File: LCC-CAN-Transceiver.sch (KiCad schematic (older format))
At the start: 19 parts

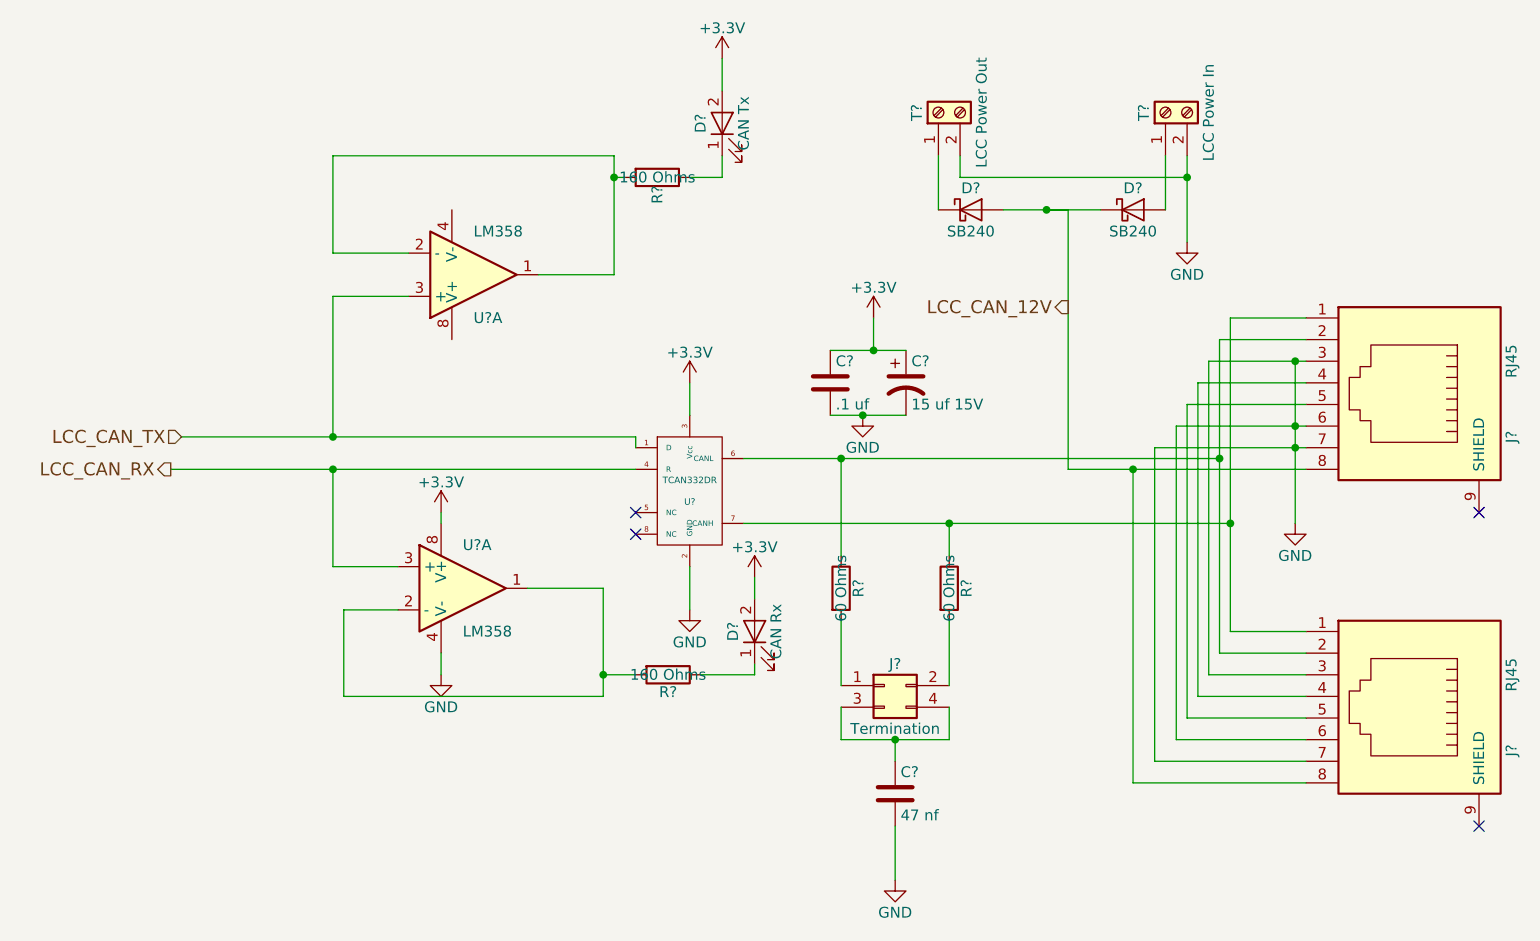
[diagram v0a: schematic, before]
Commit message: Start on LCC <=> PNET router.
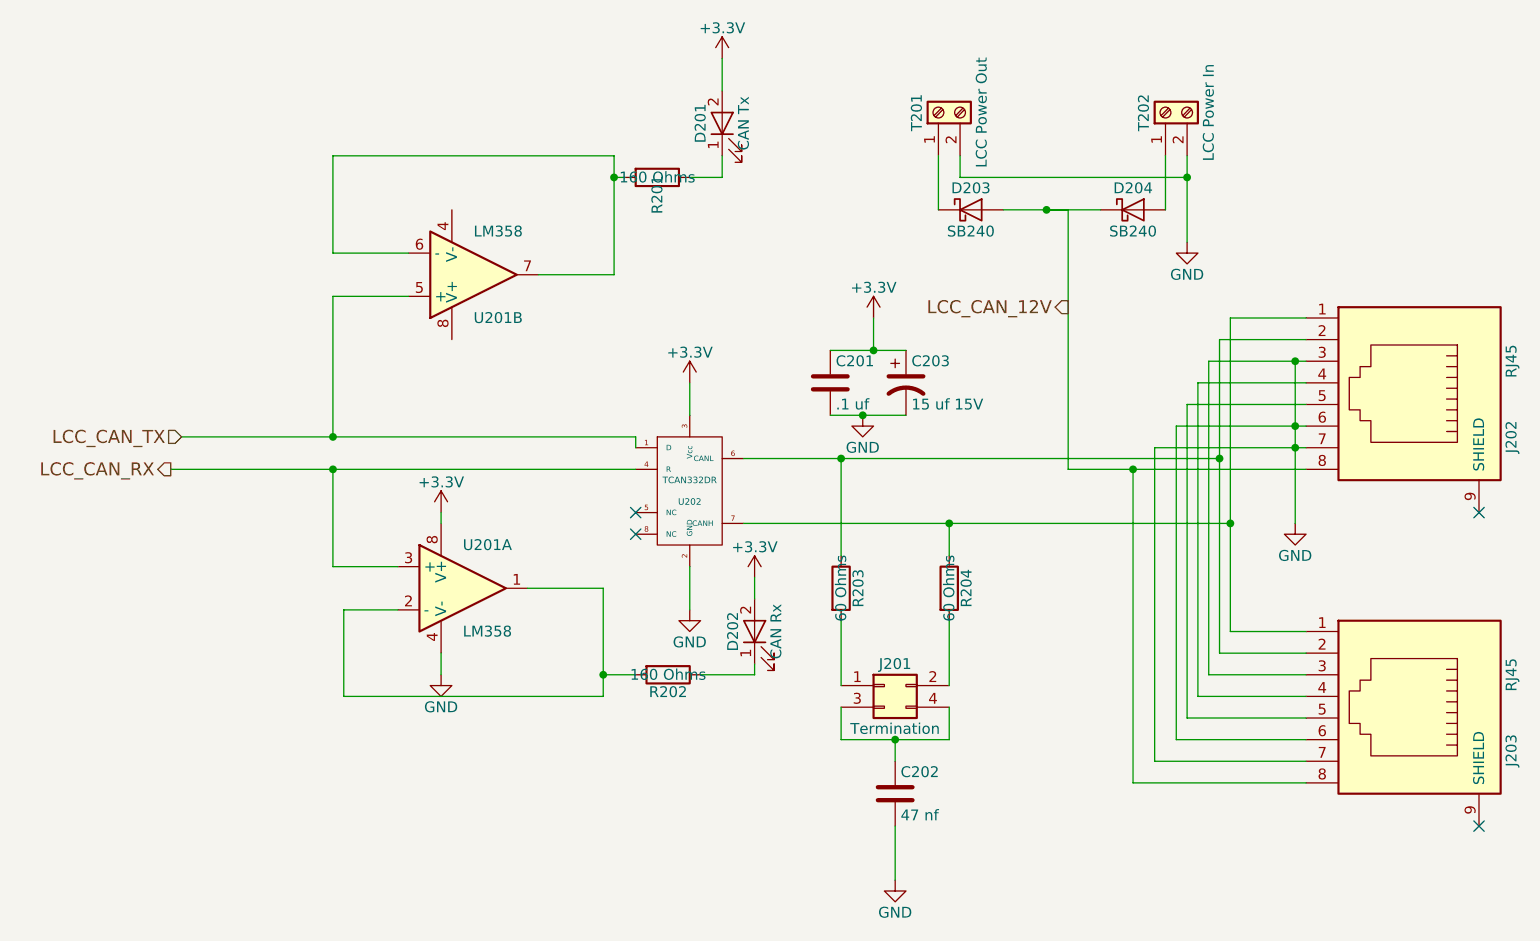
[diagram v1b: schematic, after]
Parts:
- gave numbers to parts that had none: 18
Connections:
- net LCC_CAN_TX: now also U201.5 (+); no longer U201.3 (+)
- new net: R201.2, U201.6 (-), U201.7
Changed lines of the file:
@@
 $EndDescr
 $Comp
-L TCAN332DR U?
+L TCAN332DR U202
 U 1 1 63C03309
 P 4600 2950
-F 0 "U?" H 4600 2900 30  0000 C CNN
+F 0 "U202" H 4600 2900 30  0000 C CNN
 F 1 "TCAN332DR" H 4600 3000 30  0000 C CNN
 F 2 "Housings_SOIC:SOIC-8-1EP_3.9x4.9mm_Pitch1.27mm" H 4600 2950 60  0001 C CNN
@@
 $EndComp
 $Comp
-L RJ45 J?
+L RJ45 J203
 U 1 1 63C0330A
 P 7900 3950
-F 0 "J?" H 8100 4450 50  0000 C CNN
+F 0 "J203" H 8100 4450 50  0000 C CNN
 F 1 "RJ45" H 7750 4450 50  0000 C CNN
 F 2 "RJ45-8N-S:RJ45_8N-S" H 7900 3950 50  0001 C CNN
@@
 $EndComp
 $Comp
-L RJ45 J?
+L RJ45 J202
 U 1 1 63C0330B
 P 7900 2500
-F 0 "J?" H 8100 3000 50  0000 C CNN
+F 0 "J202" H 8100 3000 50  0000 C CNN
 F 1 "RJ45" H 7750 3000 50  0000 C CNN
 F 2 "RJ45-8N-S:RJ45_8N-S" H 7900 2500 50  0001 C CNN
@@
 NoConn ~ 4350 3150
 $Comp
-L +3.3V #PWR?
+L +3.3V #PWR08
 U 1 1 63C0330C
 P 4600 2450
-F 0 "#PWR?" H 4600 2300 50  0001 C CNN
+F 0 "#PWR08" H 4600 2300 50  0001 C CNN
 F 1 "+3.3V" H 4600 2590 50  0000 C CNN
 F 2 "" H 4600 2450 50  0001 C CNN
@@
 $EndComp
 $Comp
-L GND #PWR?
+L GND #PWR09
 U 1 1 63C0330D
 P 4600 3500
-F 0 "#PWR?" H 4600 3250 50  0001 C CNN
+F 0 "#PWR09" H 4600 3250 50  0001 C CNN
 F 1 "GND" H 4600 3350 50  0000 C CNN
 F 2 "" H 4600 3500 50  0001 C CNN
@@
 $EndComp
 $Comp
-L GND #PWR?
+L GND #PWR010
 U 1 1 63C0330E
 P 7400 3100
-F 0 "#PWR?" H 7400 2850 50  0001 C CNN
+F 0 "#PWR010" H 7400 2850 50  0001 C CNN
 F 1 "GND" H 7400 2950 50  0000 C CNN
 F 2 "" H 7400 3100 50  0001 C CNN
@@
 $EndComp
 $Comp
-L C C?
+L C C201
 U 1 1 63C0330F
 P 5250 2450
-F 0 "C?" H 5275 2550 50  0000 L CNN
+F 0 "C201" H 5275 2550 50  0000 L CNN
 F 1 ".1 uf" H 5275 2350 50  0000 L CNN
 F 2 "Capacitors_THT:C_Rect_L4.0mm_W2.5mm_P2.50mm" H 5288 2300 50  0001 C CNN
@@
 $EndComp
 $Comp
-L CP1 C?
+L CP1 C203
 U 1 1 63C03310
 P 5600 2450
-F 0 "C?" H 5625 2550 50  0000 L CNN
+F 0 "C203" H 5625 2550 50  0000 L CNN
 F 1 "15 uf 15V" H 5625 2350 50  0000 L CNN
 F 2 "Capacitors_THT:CP_Radial_D6.3mm_P2.50mm" H 5600 2450 50  0001 C CNN
@@
 $EndComp
 $Comp
-L Conn_02x02_Odd_Even J?
+L Conn_02x02_Odd_Even J201
 U 1 1 63C03311
 P 5500 3850
-F 0 "J?" H 5550 3950 50  0000 C CNN
+F 0 "J201" H 5550 3950 50  0000 C CNN
 F 1 "Termination" H 5550 3650 50  0000 C CNN
 F 2 "Pin_Headers:Pin_Header_Straight_2x02_Pitch2.54mm" H 5500 3850 50  0001 C CNN
@@
 $EndComp
 $Comp
-L R R?
+L R R203
 U 1 1 63C03312
 P 5300 3400
-F 0 "R?" V 5380 3400 50  0000 C CNN
+F 0 "R203" V 5380 3400 50  0000 C CNN
 F 1 "60 Ohms" V 5300 3400 50  0000 C CNN
 F 2 "Resistors_THT:R_Axial_DIN0204_L3.6mm_D1.6mm_P2.54mm_Vertical" V 5230 3400 50  0001 C CNN
@@
 $EndComp
 $Comp
-L R R?
+L R R204
 U 1 1 63C03313
 P 5800 3400
-F 0 "R?" V 5880 3400 50  0000 C CNN
+F 0 "R204" V 5880 3400 50  0000 C CNN
 F 1 "60 Ohms" V 5800 3400 50  0000 C CNN
 F 2 "Resistors_THT:R_Axial_DIN0204_L3.6mm_D1.6mm_P2.54mm_Vertical" V 5730 3400 50  0001 C CNN
@@
 $EndComp
 $Comp
-L C C?
+L C C202
 U 1 1 63C03314
 P 5550 4350
-F 0 "C?" H 5575 4450 50  0000 L CNN
+F 0 "C202" H 5575 4450 50  0000 L CNN
 F 1 "47 nf" H 5575 4250 50  0000 L CNN
 F 2 "Capacitors_THT:C_Rect_L4.0mm_W2.5mm_P2.50mm" H 5588 4200 50  0001 C CNN
@@
 $EndComp
 $Comp
-L GND #PWR?
+L GND #PWR011
 U 1 1 63C03315
 P 5550 4750
-F 0 "#PWR?" H 5550 4500 50  0001 C CNN
+F 0 "#PWR011" H 5550 4500 50  0001 C CNN
 F 1 "GND" H 5550 4600 50  0000 C CNN
 F 2 "" H 5550 4750 50  0001 C CNN
@@
 $EndComp
 $Comp
-L +3.3V #PWR?
+L +3.3V #PWR012
 U 1 1 63C03316
 P 5450 2150
-F 0 "#PWR?" H 5450 2000 50  0001 C CNN
+F 0 "#PWR012" H 5450 2000 50  0001 C CNN
 F 1 "+3.3V" H 5450 2290 50  0000 C CNN
 F 2 "" H 5450 2150 50  0001 C CNN
@@
 $EndComp
 $Comp
-L GND #PWR?
+L GND #PWR013
 U 1 1 63C03317
 P 5400 2600
-F 0 "#PWR?" H 5400 2350 50  0001 C CNN
+F 0 "#PWR013" H 5400 2350 50  0001 C CNN
 F 1 "GND" H 5400 2450 50  0000 C CNN
 F 2 "" H 5400 2600 50  0001 C CNN
@@
 LCC_CAN_RX
 $Comp
-L Screw_Terminal_01x02 T?
+L Screw_Terminal_01x02 T201
 U 1 1 63C03318
 P 5750 1200
-F 0 "T?" H 5750 1300 50  0000 C CNN
+F 0 "T201" H 5750 1300 50  0000 C CNN
 F 1 "LCC Power Out" H 5750 1000 50  0000 C CNN
 F 2 "Connectors_Terminal_Blocks:TerminalBlock_Pheonix_MPT-2.54mm_2pol" H 5750 1200 50  0001 C CNN
@@
 $EndComp
 $Comp
-L Screw_Terminal_01x02 T?
+L Screw_Terminal_01x02 T202
 U 1 1 63C03319
 P 6800 1200
-F 0 "T?" H 6800 1300 50  0000 C CNN
+F 0 "T202" H 6800 1300 50  0000 C CNN
 F 1 "LCC Power In" H 6800 1000 50  0000 C CNN
 F 2 "Connectors_Terminal_Blocks:TerminalBlock_Pheonix_MPT-2.54mm_2pol" H 6800 1200 50  0001 C CNN
@@
 $EndComp
 $Comp
-L D_Schottky D?
+L D_Schottky D203
 U 1 1 63C0331A
 P 5900 1650
-F 0 "D?" H 5900 1750 50  0000 C CNN
+F 0 "D203" H 5900 1750 50  0000 C CNN
 F 1 "SB240" H 5900 1550 50  0000 C CNN
 F 2 "Diodes_THT:D_DO-15_P10.16mm_Horizontal" H 5900 1650 50  0001 C CNN
@@
 $EndComp
 $Comp
-L D_Schottky D?
+L D_Schottky D204
 U 1 1 63C0331B
 P 6650 1650
-F 0 "D?" H 6650 1750 50  0000 C CNN
+F 0 "D204" H 6650 1750 50  0000 C CNN
 F 1 "SB240" H 6650 1550 50  0000 C CNN
 F 2 "Diodes_THT:D_DO-15_P10.16mm_Horizontal" H 6650 1650 50  0001 C CNN
@@
 $EndComp
 $Comp
-L GND #PWR?
+L GND #PWR014
 U 1 1 63C0331C
 P 6900 1800
-F 0 "#PWR?" H 6900 1550 50  0001 C CNN
+F 0 "#PWR014" H 6900 1550 50  0001 C CNN
 F 1 "GND" H 6900 1650 50  0000 C CNN
 F 2 "" H 6900 1800 50  0001 C CNN
@@
 $EndComp
 $Comp
-L LM358 U?
-U 1 1 63C0331D
+L LM358 U201
+U 2 1 63C0331D
 P 3600 1950
-F 0 "U?" H 3600 2150 50  0000 L CNN
+F 0 "U201" H 3600 2150 50  0000 L CNN
 F 1 "LM358" H 3600 1750 50  0000 L CNN
 F 2 "Housings_DIP:DIP-8_W7.62mm" H 3600 1950 50  0001 C CNN
 F 3 "" H 3600 1950 50  0001 C CNN
 F 4 "595-LM358AP" H 3600 1950 60  0001 C CNN "Mouser Part Number"
-	1    3600 1950
+	2    3600 1950
 	1    0    0    1
 $EndComp
 $Comp
-L LM358 U?
+L LM358 U201
 U 1 1 63C0331E
 P 3550 3400
-F 0 "U?" H 3550 3600 50  0000 L CNN
+F 0 "U201" H 3550 3600 50  0000 L CNN
 F 1 "LM358" H 3550 3200 50  0000 L CNN
 F 2 "Housings_DIP:DIP-8_W7.62mm" H 3550 3400 50  0001 C CNN
@@
 $EndComp
 $Comp
-L GND #PWR?
+L GND #PWR015
 U 1 1 63C0331F
 P 3450 3800
-F 0 "#PWR?" H 3450 3550 50  0001 C CNN
+F 0 "#PWR015" H 3450 3550 50  0001 C CNN
 F 1 "GND" H 3450 3650 50  0000 C CNN
 F 2 "" H 3450 3800 50  0001 C CNN
@@
 $EndComp
 $Comp
-L +3.3V #PWR?
+L +3.3V #PWR016
 U 1 1 63C03320
 P 3450 3050
-F 0 "#PWR?" H 3450 2900 50  0001 C CNN
+F 0 "#PWR016" H 3450 2900 50  0001 C CNN
 F 1 "+3.3V" H 3450 3190 50  0000 C CNN
 F 2 "" H 3450 3050 50  0001 C CNN
@@
 $EndComp
 $Comp
-L R R?
+L R R201
 U 1 1 63C03321
 P 4450 1500
-F 0 "R?" H 4530 1500 50  0000 C CNN
+F 0 "R201" H 4530 1500 50  0000 C CNN
 F 1 "160 Ohms" V 4450 1500 50  0000 C CNN
 F 2 "Resistors_THT:R_Axial_DIN0204_L3.6mm_D1.6mm_P1.90mm_Vertical" V 4380 1500 50  0001 C CNN
@@
 $EndComp
 $Comp
-L R R?
+L R R202
 U 1 1 63C03322
 P 4500 3800
-F 0 "R?" V 4580 3800 50  0000 C CNN
+F 0 "R202" V 4580 3800 50  0000 C CNN
 F 1 "160 Ohms" V 4500 3800 50  0000 C CNN
 F 2 "Resistors_THT:R_Axial_DIN0204_L3.6mm_D1.6mm_P1.90mm_Vertical" V 4430 3800 50  0001 C CNN
@@
 $EndComp
 $Comp
-L LED D?
+L LED D201
 U 1 1 63C03323
 P 4750 1250
-F 0 "D?" H 4750 1350 50  0000 C CNN
+F 0 "D201" H 4750 1350 50  0000 C CNN
 F 1 "CAN Tx" H 4750 1150 50  0000 C CNN
 F 2 "LEDs:LED_D3.0mm" H 4750 1250 50  0001 C CNN
@@
 $EndComp
 $Comp
-L LED D?
+L LED D202
 U 1 1 63C03324
 P 4900 3600
-F 0 "D?" H 4900 3700 50  0000 C CNN
+F 0 "D202" H 4900 3700 50  0000 C CNN
 F 1 "CAN Rx" H 4900 3500 50  0000 C CNN
 F 2 "LEDs:LED_D3.0mm" H 4900 3600 50  0001 C CNN
@@
 	4900 3800 4650 3800
 $Comp
-L +3.3V #PWR?
+L +3.3V #PWR017
 U 1 1 63C03325
 P 4750 950
-F 0 "#PWR?" H 4750 800 50  0001 C CNN
+F 0 "#PWR017" H 4750 800 50  0001 C CNN
 F 1 "+3.3V" H 4750 1090 50  0000 C CNN
 F 2 "" H 4750 950 50  0001 C CNN
@@
 $EndComp
 $Comp
-L +3.3V #PWR?
+L +3.3V #PWR018
 U 1 1 63C03326
 P 4900 3350
-F 0 "#PWR?" H 4900 3200 50  0001 C CNN
+F 0 "#PWR018" H 4900 3200 50  0001 C CNN
 F 1 "+3.3V" H 4900 3490 50  0000 C CNN
 F 2 "" H 4900 3350 50  0001 C CNN
